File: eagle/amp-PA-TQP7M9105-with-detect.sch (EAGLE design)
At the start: 46 parts, among them J1 142-0701-851, J2 142-0701-851, Q1 P-CH, Q2 N-CH, U1 TQP7M9105, U2 BDCN-20-13+, U3 LT5534, U4 LT5534

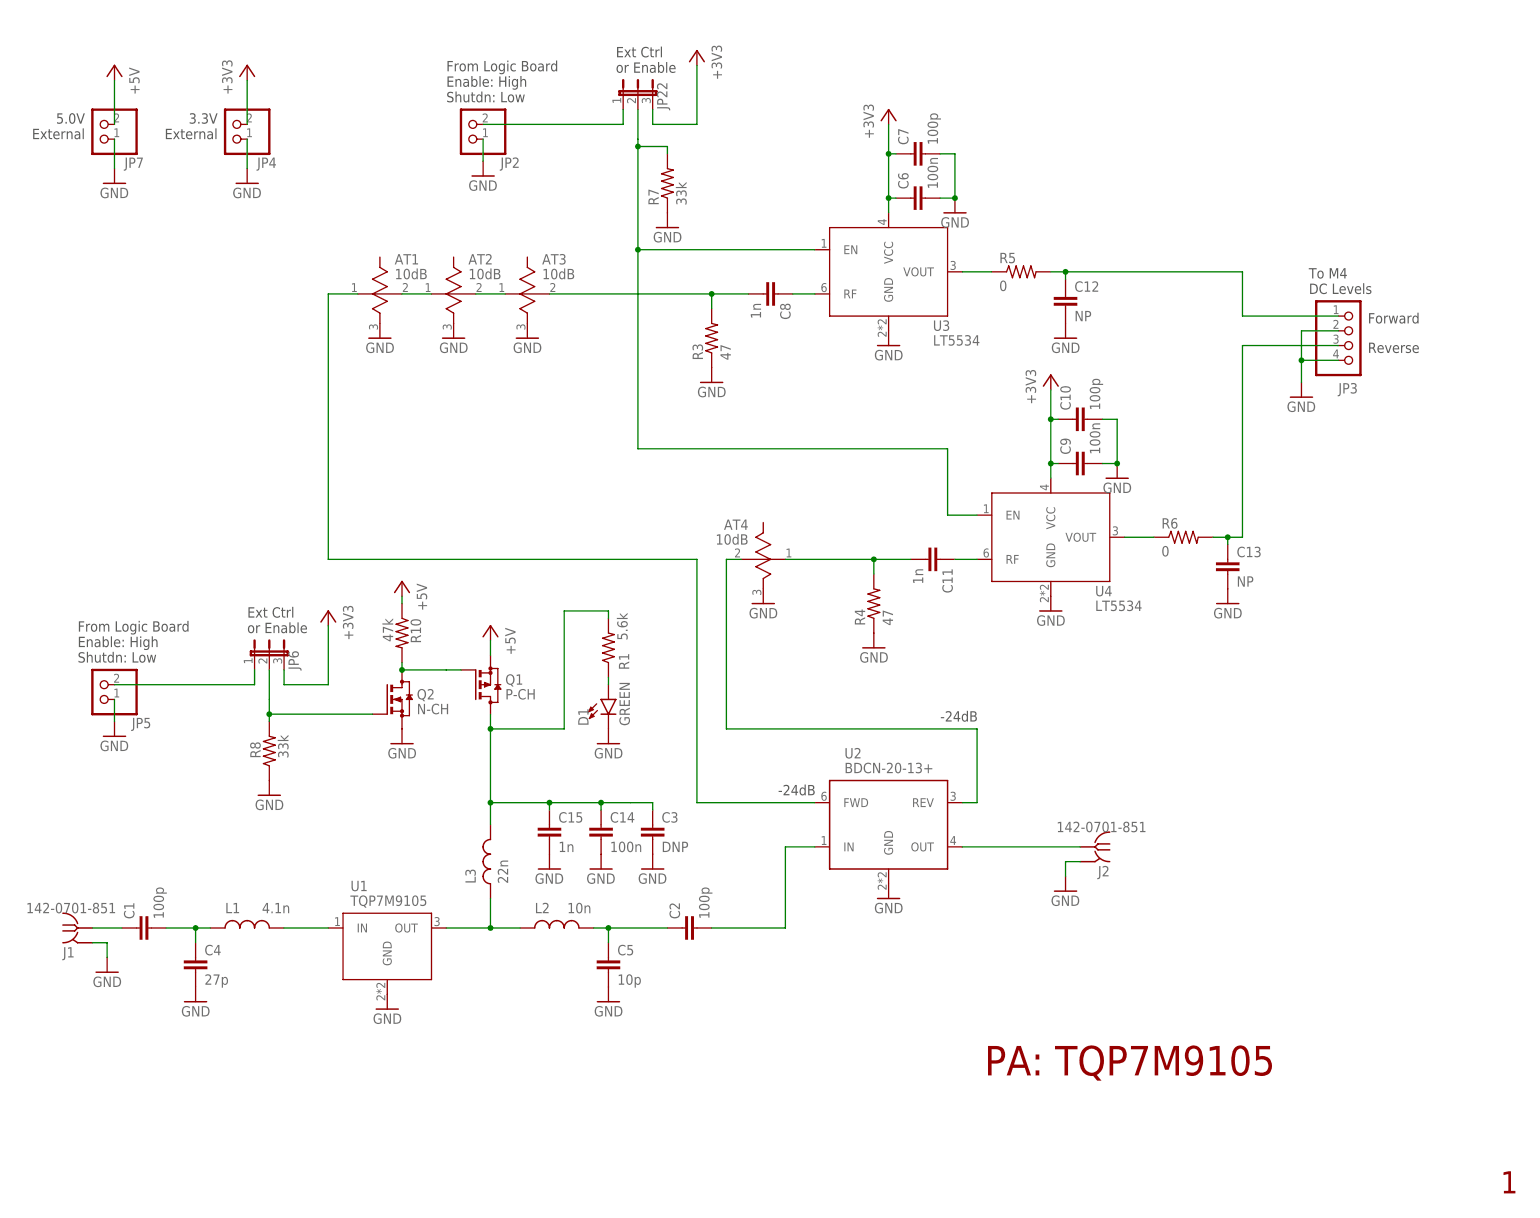
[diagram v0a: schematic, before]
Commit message: Update PA TQP7M9105 schematic
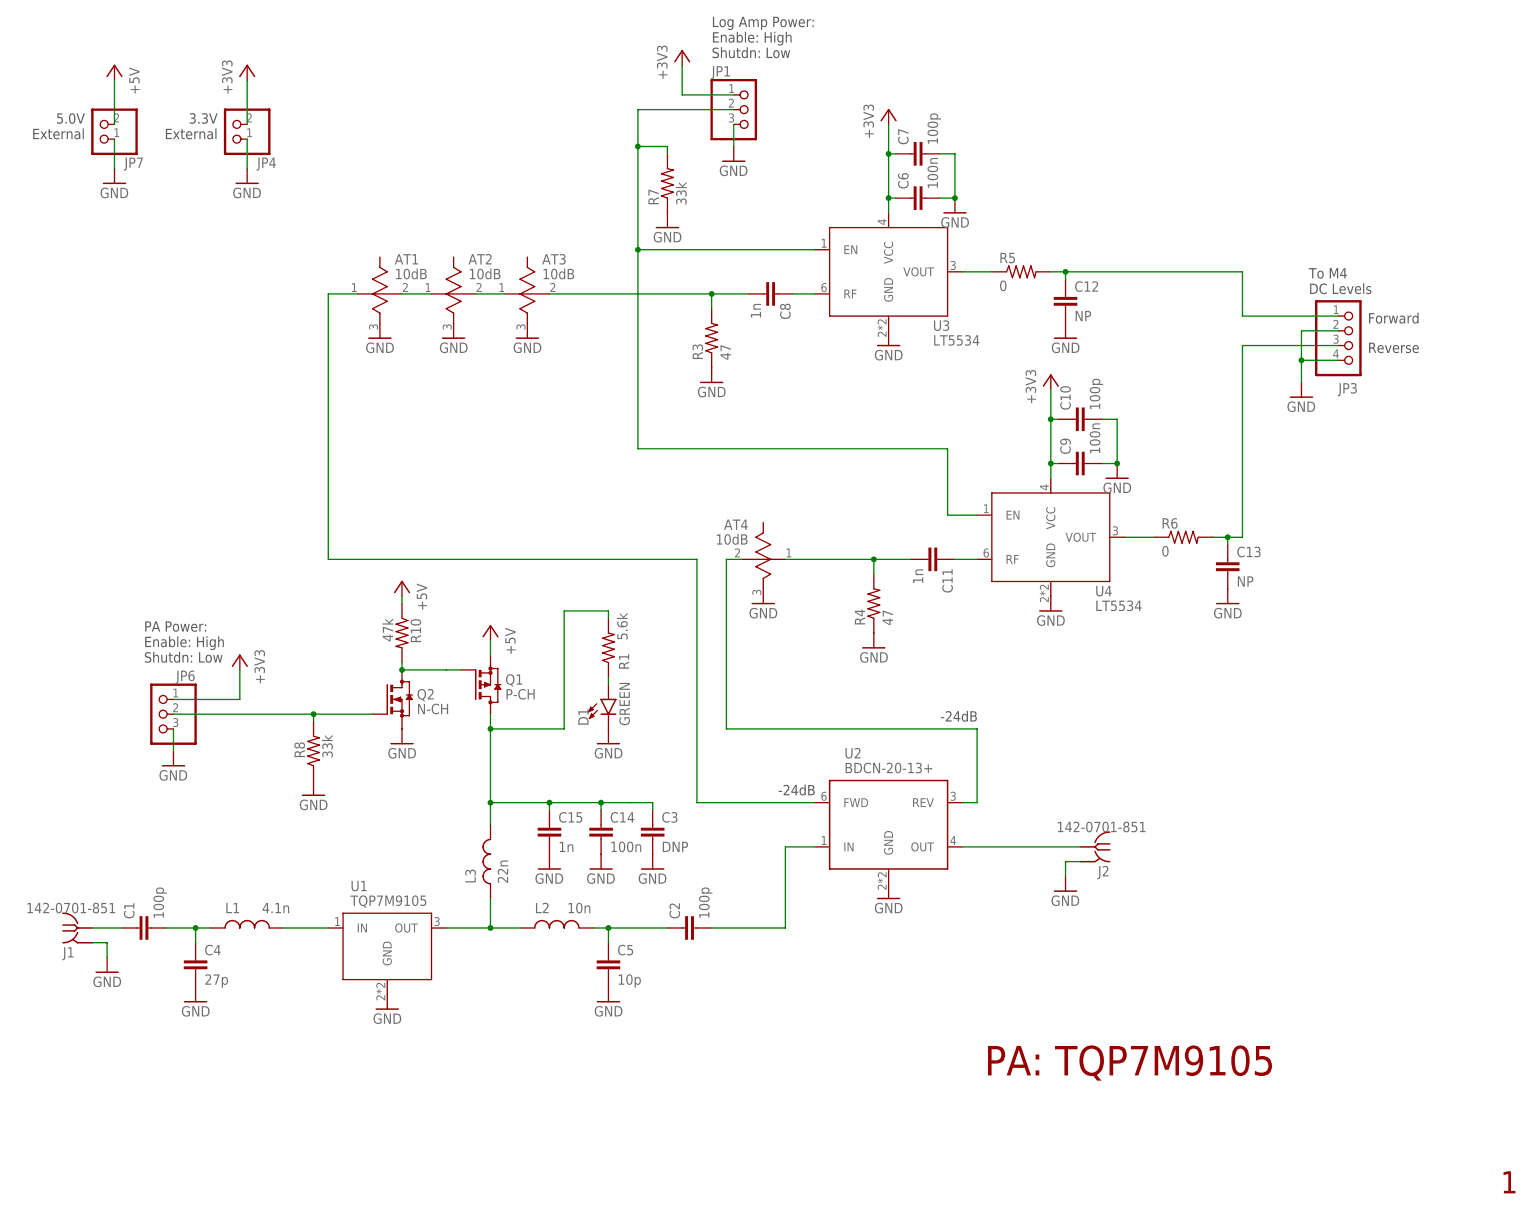
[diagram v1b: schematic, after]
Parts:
- removed JP2, JP5: (no value), pinhead:PINHD-1X2
- removed JP22: (no value), jumper:JP2E
- added JP1: (no value), pinhead:PINHD-1X3
- JP6: device jumper:JP2E -> pinhead:PINHD-1X3
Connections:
- removed net N$11: JP2.2, JP22.1
- removed net N$25 (its old number): JP5.2, JP6.1
- net +3V3: now also JP1.1, JP6.1; no longer JP22.3, JP6.3
- net GND: now also JP1.3, JP6.3; no longer JP2.1, JP5.1
- net N$10: now also JP1.2; no longer JP22.2
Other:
- note added: "Log Amp Power: Enable: High Shutdn: Low"
- note added: "PA Power: Enable: High Shutdn: Low"
- note removed: "Ext Ctrl or Enable"
- note removed: "From Logic Board Enable: High Shutdn: Low"
- moved on the sheet: R8

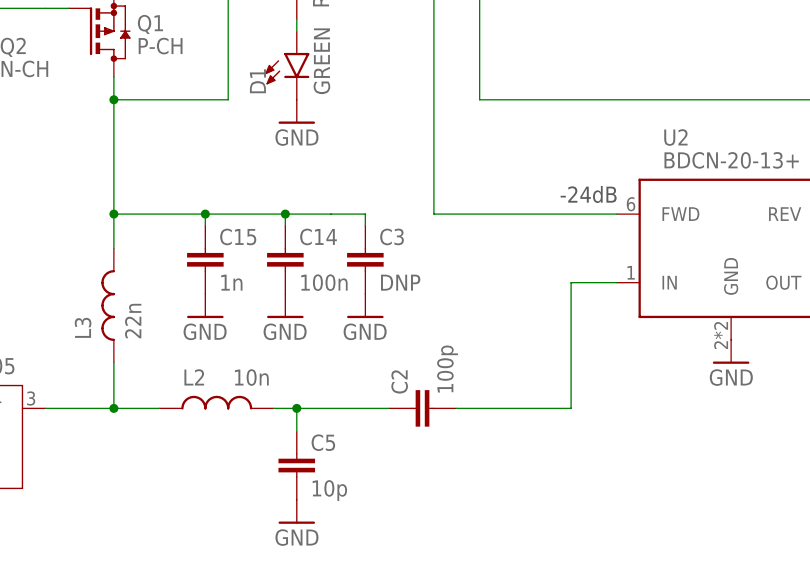
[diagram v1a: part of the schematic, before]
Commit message: Update PA layout placement
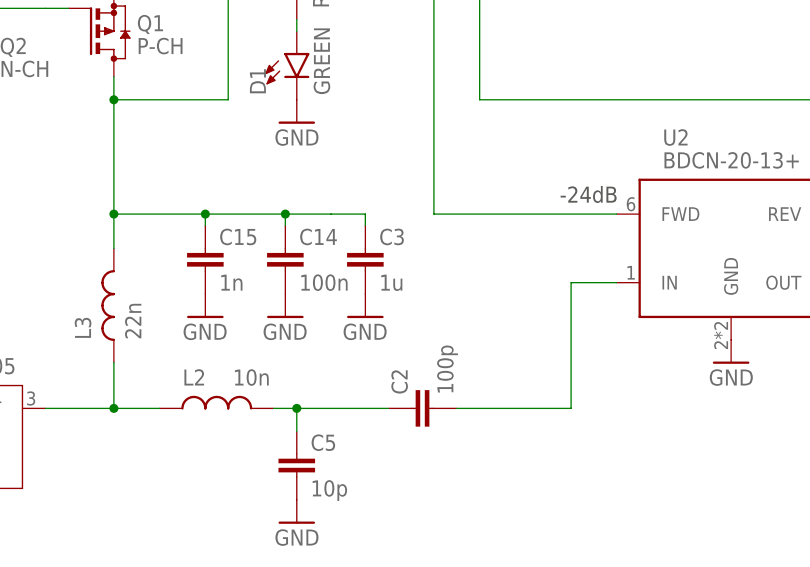
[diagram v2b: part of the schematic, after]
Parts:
- C3: value DNP -> 1u
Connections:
- net N$14 renamed FWD
- net N$15 renamed REV
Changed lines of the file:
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@@
 <part name="R8" library="oresat-rcl" deviceset="R-US_" device="0402-B-NOSILK" value="33k"/>
 <part name="GND25" library="supply1" library_urn="urn:adsk.eagle:library:371" deviceset="GND" device=""/>
-<part name="C3" library="oresat-rcl" deviceset="C-EU" device="0603-B-NOSILK" value="DNP"/>
+<part name="C3" library="oresat-rcl" deviceset="C-EU" device="0603-B-NOSILK" value="1u"/>
 <part name="C14" library="oresat-rcl" deviceset="C-EU" device="0603-B-NOSILK" value="100n"/>
 <part name="C15" library="oresat-rcl" deviceset="C-EU" device="0603-B-NOSILK" value="1n"/>
@@
 </segment>
 </net>
-<net name="N$14" class="0">
+<net name="FWD" class="0">
 <segment>
 <pinref part="JP3" gate="A" pin="1"/>
@@
 </segment>
 </net>
-<net name="N$15" class="0">
+<net name="REV" class="0">
 <segment>
 <pinref part="JP3" gate="A" pin="3"/>

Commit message: Update PA TQP7M9105 layout
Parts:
- removed JP7: (no value), pinhead:PINHD-1X2
- added JP5: (no value), pinhead:PINHD-1X4
- JP3: device pinhead:PINHD-1X4 -> pinhead:PINHD-1X2
- renumbered JP6 to JP2
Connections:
- net N$19 renamed CAPS
- net +5V: now also JP3.2; no longer JP7.2
- net FWD: now also JP5.1; no longer JP3.1
- net GND: now also JP3.1, JP5.2, JP5.4; no longer JP3.2, JP3.4, JP7.1
- net REV: now also JP5.3; no longer JP3.3
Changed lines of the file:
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@@
 <part name="R4" library="oresat-rcl" deviceset="R-US_" device="0402-C-NOSILK" value="47"/>
 <part name="GND15" library="supply1" library_urn="urn:adsk.eagle:library:371" deviceset="GND" device=""/>
-<part name="JP3" library="pinhead" library_urn="urn:adsk.eagle:library:325" deviceset="PINHD-1X4" device="" package3d_urn="urn:adsk.eagle:package:22407/2"/>
+<part name="JP5" library="pinhead" library_urn="urn:adsk.eagle:library:325" deviceset="PINHD-1X4" device="" package3d_urn="urn:adsk.eagle:package:22407/2"/>
 <part name="GND16" library="supply1" library_urn="urn:adsk.eagle:library:371" deviceset="GND" device=""/>
 <part name="AT1" library="AT-Susumu-PAT-attenuator" deviceset="PAT1220" device="" value="10dB"/>
@@
 <part name="GND8" library="supply1" library_urn="urn:adsk.eagle:library:371" deviceset="GND" device=""/>
 <part name="+3V4" library="supply1" library_urn="urn:adsk.eagle:library:371" deviceset="+3V3" device=""/>
-<part name="JP7" library="pinhead" library_urn="urn:adsk.eagle:library:325" deviceset="PINHD-1X2" device="" package3d_urn="urn:adsk.eagle:package:22435/2"/>
+<part name="JP3" library="pinhead" library_urn="urn:adsk.eagle:library:325" deviceset="PINHD-1X2" device="" package3d_urn="urn:adsk.eagle:package:22435/2"/>
 <part name="GND24" library="supply1" library_urn="urn:adsk.eagle:library:371" deviceset="GND" device=""/>
 <part name="P+3" library="supply1" library_urn="urn:adsk.eagle:library:371" deviceset="+5V" device=""/>
@@
 <part name="GND26" library="supply1" library_urn="urn:adsk.eagle:library:371" deviceset="GND" device=""/>
 <part name="JP1" library="pinhead" library_urn="urn:adsk.eagle:library:325" deviceset="PINHD-1X3" device="" package3d_urn="urn:adsk.eagle:package:22458/2"/>
-<part name="JP6" library="pinhead" library_urn="urn:adsk.eagle:library:325" deviceset="PINHD-1X3" device="" package3d_urn="urn:adsk.eagle:package:22458/2"/>
+<part name="JP2" library="pinhead" library_urn="urn:adsk.eagle:library:325" deviceset="PINHD-1X3" device="" package3d_urn="urn:adsk.eagle:package:22458/2"/>
 <part name="GND11" library="supply1" library_urn="urn:adsk.eagle:library:371" deviceset="GND" device=""/>
 </parts>
@@
 <attribute name="VALUE" x="160.02" y="97.79" size="1.778" layer="96" rot="MR0"/>
 </instance>
-<instance part="JP3" gate="A" x="240.03" y="152.4" smashed="yes">
+<instance part="JP5" gate="A" x="240.03" y="152.4" smashed="yes">
 <attribute name="NAME" x="237.49" y="144.145" size="1.778" layer="95"/>
 <attribute name="VALUE" x="233.68" y="144.78" size="1.778" layer="96"/>
@@
 <attribute name="VALUE" x="50.8" y="93.98" size="1.778" layer="96" rot="MR90"/>
 </instance>
-<instance part="JP7" gate="G$1" x="24.13" y="190.5" smashed="yes" rot="R180">
+<instance part="JP3" gate="G$1" x="24.13" y="190.5" smashed="yes" rot="R180">
 <attribute name="NAME" x="31.75" y="184.785" size="1.778" layer="95" rot="R180"/>
 <attribute name="VALUE" x="30.48" y="195.58" size="1.778" layer="96" rot="R180"/>
@@
 <attribute name="VALUE" x="129.54" y="185.42" size="1.778" layer="96"/>
 </instance>
-<instance part="JP6" gate="A" x="34.29" y="88.9" smashed="yes" rot="MR0">
+<instance part="JP2" gate="A" x="34.29" y="88.9" smashed="yes" rot="MR0">
 <attribute name="NAME" x="40.64" y="94.615" size="1.778" layer="95" rot="MR0"/>
 <attribute name="VALUE" x="40.64" y="81.28" size="1.778" layer="96" rot="MR0"/>
@@
 </segment>
 <segment>
-<pinref part="JP3" gate="A" pin="4"/>
+<pinref part="JP5" gate="A" pin="4"/>
 <pinref part="GND16" gate="1" pin="GND"/>
 <wire x1="237.49" y1="149.86" x2="231.14" y2="149.86" width="0.1524" layer="91"/>
 <wire x1="231.14" y1="149.86" x2="231.14" y2="146.05" width="0.1524" layer="91"/>
-<pinref part="JP3" gate="A" pin="2"/>
+<pinref part="JP5" gate="A" pin="2"/>
 <wire x1="237.49" y1="154.94" x2="231.14" y2="154.94" width="0.1524" layer="91"/>
 <wire x1="231.14" y1="154.94" x2="231.14" y2="149.86" width="0.1524" layer="91"/>
@@
 <wire x1="36.83" y1="86.36" x2="36.83" y2="82.55" width="0.1524" layer="91"/>
 <pinref part="GND8" gate="1" pin="GND"/>
-<pinref part="JP6" gate="A" pin="3"/>
+<pinref part="JP2" gate="A" pin="3"/>
 </segment>
 <segment>
 <pinref part="GND24" gate="1" pin="GND"/>
-<pinref part="JP7" gate="G$1" pin="1"/>
+<pinref part="JP3" gate="G$1" pin="1"/>
 <wire x1="26.67" y1="182.88" x2="26.67" y2="187.96" width="0.1524" layer="91"/>
 </segment>
@@
 </segment>
 </net>
-<net name="N$1" class="0">
+<net name="N$1" class="2">
 <segment>
 <pinref part="J1" gate="G$1" pin="RF"/>
@@
 </segment>
 </net>
-<net name="N$3" class="0">
+<net name="N$3" class="2">
 <segment>
 <pinref part="C1" gate="CE" pin="2"/>
@@
 </segment>
 </net>
-<net name="N$4" class="0">
+<net name="N$4" class="2">
 <segment>
 <pinref part="L1" gate="L" pin="2"/>
@@
 </segment>
 </net>
-<net name="N$5" class="0">
+<net name="N$5" class="2">
 <segment>
 <pinref part="L2" gate="L" pin="1"/>
@@
 </segment>
 </net>
-<net name="N$6" class="0">
+<net name="N$6" class="2">
 <segment>
 <pinref part="L2" gate="L" pin="2"/>
@@
 <segment>
 <pinref part="+3V4" gate="G$1" pin="+3V3"/>
-<pinref part="JP6" gate="A" pin="1"/>
+<pinref part="JP2" gate="A" pin="1"/>
 <wire x1="48.26" y1="96.52" x2="48.26" y2="91.44" width="0.1524" layer="91"/>
 <wire x1="48.26" y1="91.44" x2="36.83" y2="91.44" width="0.1524" layer="91"/>
 </segment>
 </net>
-<net name="N$8" class="0">
+<net name="N$8" class="1">
 <segment>
 <pinref part="C8" gate="CE" pin="1"/>
@@
 </segment>
 </net>
-<net name="N$9" class="0">
+<net name="N$9" class="1">
 <segment>
 <pinref part="R3" gate="R" pin="2"/>
@@
 </segment>
 </net>
-<net name="N$12" class="0">
+<net name="N$12" class="1">
 <segment>
 <pinref part="C11" gate="CE" pin="1"/>
@@
 </segment>
 </net>
-<net name="N$13" class="0">
+<net name="N$13" class="1">
 <segment>
 <pinref part="R4" gate="R" pin="2"/>
@@
 <net name="FWD" class="0">
 <segment>
-<pinref part="JP3" gate="A" pin="1"/>
+<pinref part="JP5" gate="A" pin="1"/>
 <wire x1="237.49" y1="157.48" x2="220.98" y2="157.48" width="0.1524" layer="91"/>
 <wire x1="220.98" y1="157.48" x2="220.98" y2="165.1" width="0.1524" layer="91"/>
@@
 <net name="REV" class="0">
 <segment>
-<pinref part="JP3" gate="A" pin="3"/>
+<pinref part="JP5" gate="A" pin="3"/>
 <wire x1="237.49" y1="152.4" x2="220.98" y2="152.4" width="0.1524" layer="91"/>
 <wire x1="220.98" y1="152.4" x2="220.98" y2="119.38" width="0.1524" layer="91"/>
@@
 </segment>
 </net>
-<net name="N$16" class="0">
+<net name="N$16" class="1">
 <segment>
 <pinref part="AT1" gate="G$1" pin="1"/>
@@
 </segment>
 </net>
-<net name="N$17" class="0">
+<net name="N$17" class="1">
 <segment>
 <pinref part="AT1" gate="G$1" pin="2"/>
@@
 </segment>
 </net>
-<net name="N$18" class="0">
+<net name="N$18" class="1">
 <segment>
 <pinref part="AT2" gate="G$1" pin="2"/>
@@
 </segment>
 </net>
-<net name="N$2" class="0">
+<net name="N$2" class="2">
 <segment>
 <pinref part="C2" gate="CE" pin="2"/>
@@
 </segment>
 </net>
-<net name="N$7" class="0">
+<net name="N$7" class="2">
 <segment>
 <pinref part="U2" gate="G$1" pin="OUT"/>
@@
 </segment>
 </net>
-<net name="N$22" class="0">
+<net name="N$22" class="1">
 <segment>
 <wire x1="132.08" y1="115.57" x2="132.08" y2="86.36" width="0.1524" layer="91"/>
@@
 </segment>
 </net>
-<net name="N$19" class="0">
+<net name="CAPS" class="0">
 <segment>
 <pinref part="Q1" gate="G$1" pin="D"/>
@@
 </segment>
 <segment>
-<pinref part="JP7" gate="G$1" pin="2"/>
+<pinref part="JP3" gate="G$1" pin="2"/>
 <wire x1="26.67" y1="190.5" x2="26.67" y2="198.12" width="0.1524" layer="91"/>
 <pinref part="P+3" gate="1" pin="+5V"/>
@@
 <pinref part="R8" gate="R" pin="2"/>
 <wire x1="60.96" y1="87.63" x2="60.96" y2="88.9" width="0.1524" layer="91"/>
-<pinref part="JP6" gate="A" pin="2"/>
+<pinref part="JP2" gate="A" pin="2"/>
 <wire x1="36.83" y1="88.9" x2="60.96" y2="88.9" width="0.1524" layer="91"/>
 <junction x="60.96" y="88.9"/>
